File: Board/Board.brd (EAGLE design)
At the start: 53.2 x 84.2 mm, 70 parts, among them IC1 MEGA328, IC2 LM358D, IC4 MCP3426, IC6 MCP4921, IC7 TL431CD, Q1 IRLIZ44N, T1 BC817, U1 CJT1117-3.3-SOT223, U3 MCP9701AT-E/TT, U4 IRLML2502

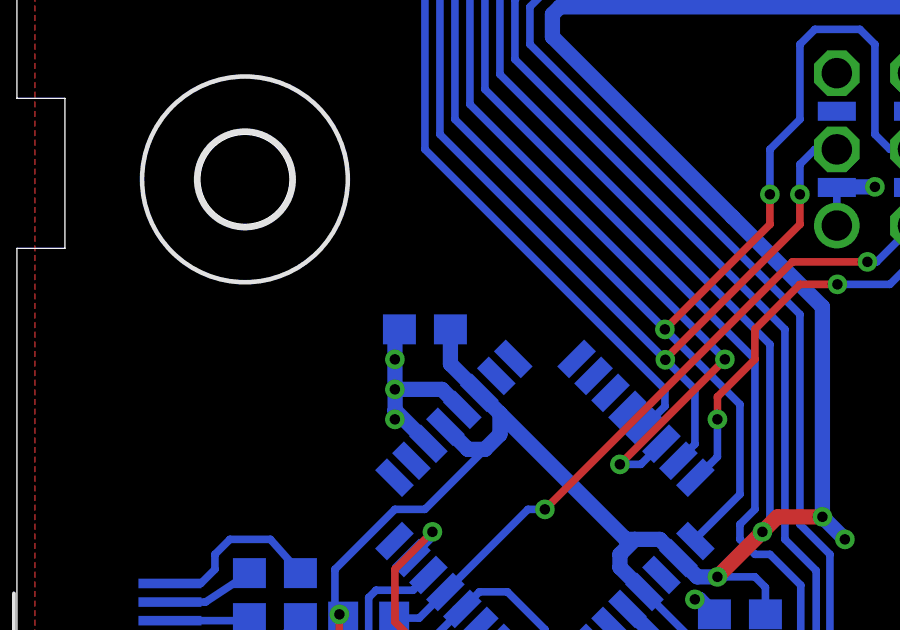
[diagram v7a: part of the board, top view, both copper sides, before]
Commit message: added testpads for XTAL1 and XTAL2
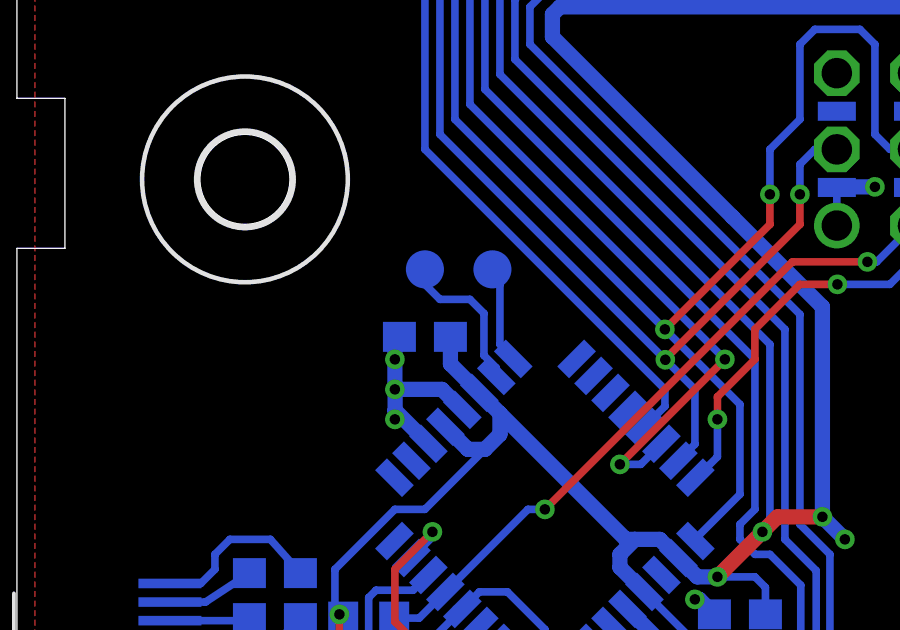
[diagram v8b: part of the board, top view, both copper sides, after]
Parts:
- added XTAL1, XTAL2: TPB1,27, testpad:B1,27
- moved U$1 3.50 mm to (34.5, 20.0)
- moved U$3 3.00 mm to (39.5, 20.5)
- moved C7 0.25 mm to (13.0, 18.8)
- renumbered SV1 to J1
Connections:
- new net N$12: IC1.8, XTAL2.TP
- new net N$13: IC1.7, XTAL1.TP
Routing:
- net N$13: track 0.00 -> 5.12 mm
- net N$12: track 0.00 -> 3.27 mm
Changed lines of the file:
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@@
 <layer number="19" name="Unrouted" color="6" fill="1" visible="yes" active="yes"/>
 <layer number="20" name="Dimension" color="24" fill="1" visible="yes" active="yes"/>
-<layer number="21" name="tPlace" color="7" fill="1" visible="no" active="yes"/>
+<layer number="21" name="tPlace" color="7" fill="1" visible="yes" active="yes"/>
 <layer number="22" name="bPlace" color="7" fill="1" visible="yes" active="yes"/>
-<layer number="23" name="tOrigins" color="15" fill="1" visible="no" active="yes"/>
+<layer number="23" name="tOrigins" color="15" fill="1" visible="yes" active="yes"/>
 <layer number="24" name="bOrigins" color="15" fill="1" visible="yes" active="yes"/>
 <layer number="25" name="tNames" color="7" fill="1" visible="no" active="yes"/>
@@
 <wire x1="31.5" y1="77.25" x2="34" y2="74.75" width="1" layer="46" curve="-90"/>
 <wire x1="34" y1="74.75" x2="31.5" y2="72.25" width="1" layer="46" curve="-90"/>
-<text x="33" y="18" size="0.6096" layer="22" rot="MR0" align="center">PocketLoad
+<text x="37" y="18" size="0.6096" layer="22" rot="MR0" align="center">PocketLoad
 by nupo-artworks.de</text>
 <text x="22" y="79.5" size="1.4224" layer="21" align="center">40V / 6A</text>
-<text x="33" y="16.5" size="0.6096" layer="22" rot="MR0" align="center">github.com/dangrie158/pocket-load</text>
+<text x="37" y="16.5" size="0.6096" layer="22" rot="MR0" align="center">github.com/dangrie158/pocket-load</text>
 </plain>
 <attributes>
@@
 <attribute name="VALUE" x="10.49" y="11.28" size="1.27" layer="28" rot="MR180"/>
 </element>
-<element name="C7" library="rcl" package="C0603" value="100n" x="13" y="19" smashed="yes" rot="MR0">
-<attribute name="NAME" x="13" y="20.25" size="0.6096" layer="26" rot="MR0" align="center"/>
-<attribute name="VALUE" x="13.634996875" y="17.094996875" size="1.27" layer="28" rot="MR0"/>
+<element name="C7" library="rcl" package="C0603" value="100n" x="13" y="18.75" smashed="yes" rot="MR0">
+<attribute name="NAME" x="13" y="20" size="0.6096" layer="26" rot="MR0" align="center"/>
+<attribute name="VALUE" x="13.634996875" y="16.844996875" size="1.27" layer="28" rot="MR0"/>
 </element>
 <element name="C8" library="rcl" package="C0603" value="100n" x="23.5" y="9.5" smashed="yes" rot="MR0">
@@
 <attribute name="VALUE" x="11.76" y="5.595" size="1.27" layer="28" rot="MR0"/>
 </element>
-<element name="U$1" library="OwnStuff" package="LOGO-SILKSCREEEN-S" value="" x="31" y="20" rot="MR0"/>
+<element name="U$1" library="OwnStuff" package="LOGO-SILKSCREEEN-S" value="" x="34.5" y="20" rot="MR0"/>
 <element name="F1" library="Seeed-OPL-fuse" package="F1206" value="6.3A/63V" x="28.75" y="66" rot="MR0"/>
-<element name="U$3" library="SparkFun-Aesthetics" package="OSHW-LOGO-S" value="" x="36.5" y="20.5" rot="MR0"/>
+<element name="U$3" library="SparkFun-Aesthetics" package="OSHW-LOGO-S" value="" x="39.5" y="20.5" rot="MR0"/>
 <element name="D3" library="SparkFun-DiscreteSemi" package="SOD-323" value="1.1V" x="35" y="66" smashed="yes" rot="MR0">
 <attribute name="NAME" x="35" y="67.25" size="0.6096" layer="26" rot="MR0" align="center"/>
@@
 <attribute name="VALUE" value="5.6V" x="36.524" y="63.587" size="1.27" layer="28" rot="MR0"/>
 </element>
-<element name="SV1" library="con-lstb" library_urn="urn:adsk.eagle:library:162" package="MA03-2" package3d_urn="urn:adsk.eagle:package:8334/1" value="" x="28" y="25" rot="MR90">
+<element name="J1" library="con-lstb" library_urn="urn:adsk.eagle:library:162" package="MA03-2" package3d_urn="urn:adsk.eagle:package:8334/1" value="" x="28" y="25" smashed="yes" rot="MR90">
 <attribute name="MF" value="" x="28" y="25" size="1.778" layer="28" rot="MR90" display="off"/>
 <attribute name="MPN" value="" x="28" y="25" size="1.778" layer="28" rot="MR90" display="off"/>
+<attribute name="NAME" x="31" y="25" size="0.6096" layer="26" ratio="10" rot="MR90" align="center"/>
 <attribute name="OC_FARNELL" value="unknown" x="28" y="25" size="1.778" layer="28" rot="MR90" display="off"/>
 <attribute name="OC_NEWARK" value="unknown" x="28" y="25" size="1.778" layer="28" rot="MR90" display="off"/>
+<attribute name="VALUE" x="23.809" y="23.73" size="1.27" layer="28" ratio="10" rot="MR90"/>
+</element>
+<element name="XTAL1" library="testpad" package="B1,27" value="TPB1,27" x="13" y="21" smashed="yes" rot="MR0">
+<attribute name="NAME" x="12.5" y="22" size="0.6096" layer="26" ratio="10" rot="MR0" align="center"/>
+<attribute name="TP_SIGNAL_NAME" value="" x="13.635" y="19.095" size="1" layer="38" rot="MR0"/>
+<attribute name="VALUE" x="13.635" y="20.238" size="0.0254" layer="28" rot="MR0"/>
+</element>
+<element name="XTAL2" library="testpad" package="B1,27" value="TPB1,27" x="15.25" y="21" smashed="yes" rot="MR0">
+<attribute name="NAME" x="15.75" y="22" size="0.6096" layer="26" ratio="10" rot="MR0" align="center"/>
+<attribute name="TP_SIGNAL_NAME" value="" x="15.885" y="19.095" size="1" layer="38" rot="MR0"/>
+<attribute name="VALUE" x="15.885" y="20.238" size="0.0254" layer="28" rot="MR0"/>
 </element>
 </elements>
@@
 <wire x1="2.978690625" y1="6.771309375" x2="3" y2="7" width="0.254" layer="1"/>
 <wire x1="12" y1="17" x2="12" y2="18" width="0.508" layer="16"/>
-<wire x1="12" y1="18.85" x2="12" y2="18" width="0.508" layer="16"/>
-<wire x1="12" y1="18.85" x2="12.15" y2="19" width="0.508" layer="16"/>
+<wire x1="12" y1="18.6" x2="12" y2="18" width="0.508" layer="16"/>
+<wire x1="12" y1="18.6" x2="12.15" y2="18.75" width="0.508" layer="16"/>
 <wire x1="14.24751875" y1="16.31816875" x2="13.5656875" y2="17" width="0.508" layer="16"/>
 <wire x1="13.5656875" y1="17" x2="12" y2="17" width="0.508" layer="16"/>
@@
 <via x="33" y="66" extent="1-16" drill="0.35"/>
 <wire x1="33.85" y1="66" x2="33" y2="66" width="0.254" layer="16"/>
-<contactref element="SV1" pad="1"/>
+<contactref element="J1" pad="1"/>
 <wire x1="26.73" y1="22.46" x2="26.73" y2="23.73" width="0.254" layer="16"/>
 <wire x1="26.73" y1="23.73" x2="26.75" y2="23.75" width="0.508" layer="16"/>
@@
 <wire x1="25.5" y1="28.5" x2="25.5" y2="26" width="0.254" layer="16"/>
 <wire x1="25.5" y1="26" x2="24.5" y2="25" width="0.254" layer="16"/>
-<contactref element="SV1" pad="4"/>
+<contactref element="J1" pad="4"/>
 </signal>
 <signal name="MOSI">
@@
 <wire x1="25.5" y1="22.5" x2="21" y2="18" width="0.254" layer="1"/>
 <wire x1="21" y1="18" x2="21.01360625" y2="17.98639375" width="0.254" layer="1"/>
-<contactref element="SV1" pad="3"/>
+<contactref element="J1" pad="3"/>
 </signal>
 <signal name="VLOAD_ATT">
@@
 <wire x1="47" y1="34.85" x2="47" y2="35.49193125" width="0.254" layer="16"/>
 <wire x1="14.813203125" y1="16.883853125" x2="13.85" y2="17.84705625" width="0.508" layer="16"/>
-<wire x1="13.85" y1="17.84705625" x2="13.85" y2="19" width="0.508" layer="16"/>
+<wire x1="13.85" y1="17.84705625" x2="13.85" y2="18.75" width="0.508" layer="16"/>
 <wire x1="40.546059375" y1="34.5" x2="42.72705" y2="34.5" width="0.508" layer="16"/>
 <wire x1="40.546059375" y1="34.5" x2="38" y2="34.5" width="0.508" layer="16"/>
@@
 <wire x1="13.68183125" y1="10.247515625" x2="16.434315625" y2="13" width="0.254" layer="16"/>
 <wire x1="16.434315625" y1="13" x2="17" y2="13" width="0.254" layer="16"/>
-<contactref element="SV1" pad="2"/>
+<contactref element="J1" pad="2"/>
 <wire x1="17" y1="13" x2="25.25" y2="21.25" width="0.254" layer="1"/>
 <wire x1="25.25" y1="21.25" x2="27.75" y2="21.25" width="0.254" layer="1"/>
@@
 <wire x1="22.75" y1="16.75" x2="24" y2="18" width="0.254" layer="1"/>
 <wire x1="24" y1="18" x2="24" y2="19" width="0.254" layer="1"/>
-<contactref element="SV1" pad="6"/>
+<contactref element="J1" pad="6"/>
 <wire x1="24" y1="19" x2="25.5" y2="20.5" width="0.254" layer="1"/>
 <wire x1="25.5" y1="20.5" x2="26.75" y2="20.5" width="0.254" layer="1"/>
@@
 </signal>
 <signal name="+5V">
-<contactref element="SV1" pad="5"/>
+<contactref element="J1" pad="5"/>
+</signal>
+<signal name="N$12">
+<contactref element="IC1" pad="8"/>
+<wire x1="15.5" y1="18.5" x2="15.944575" y2="18.055425" width="0.254" layer="16"/>
+<wire x1="15.944575" y1="18.055425" x2="15.944575" y2="18.015225" width="0.254" layer="16"/>
+<wire x1="15.5" y1="20.5" x2="15.5" y2="18.5" width="0.254" layer="16"/>
+<contactref element="XTAL2" pad="TP"/>
+<wire x1="15.25" y1="21" x2="15.25" y2="20.75" width="0.254" layer="16"/>
+<wire x1="15.25" y1="20.75" x2="15.5" y2="20.5" width="0.254" layer="16"/>
+</signal>
+<signal name="N$13">
+<contactref element="IC1" pad="7"/>
+<wire x1="15.3788875" y1="17.4495375" x2="15.3788875" y2="17.7188125" width="0.254" layer="16"/>
+<wire x1="15.3788875" y1="17.7188125" x2="14.967796875" y2="18.129903125" width="0.254" layer="16"/>
+<wire x1="14.967796875" y1="18.129903125" x2="14.967796875" y2="19.532203125" width="0.254" layer="16"/>
+<contactref element="XTAL1" pad="TP"/>
+<wire x1="14.967796875" y1="19.532203125" x2="14.5" y2="20" width="0.254" layer="16"/>
+<wire x1="14.5" y1="20" x2="13.5" y2="20" width="0.254" layer="16"/>
+<wire x1="13.5" y1="20" x2="13" y2="20.5" width="0.254" layer="16"/>
+<wire x1="13" y1="20.5" x2="13" y2="21" width="0.254" layer="16"/>
 </signal>
 </signals>
